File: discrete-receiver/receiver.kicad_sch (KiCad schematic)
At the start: 30 parts, among them J1 His Excellence, J3 External Filter, J7 Her Excellency, T1 H1102NLT, T2 MABA-007159-000000, U5 ADE-1+

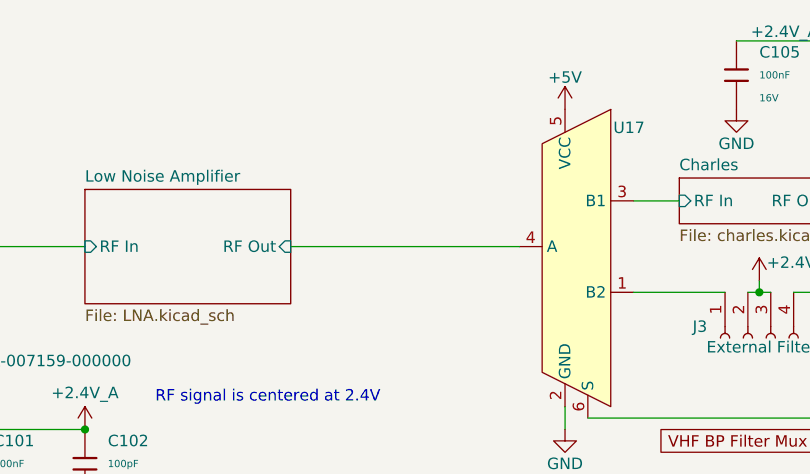
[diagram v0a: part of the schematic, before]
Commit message: Added RF recenter resistor after LNA
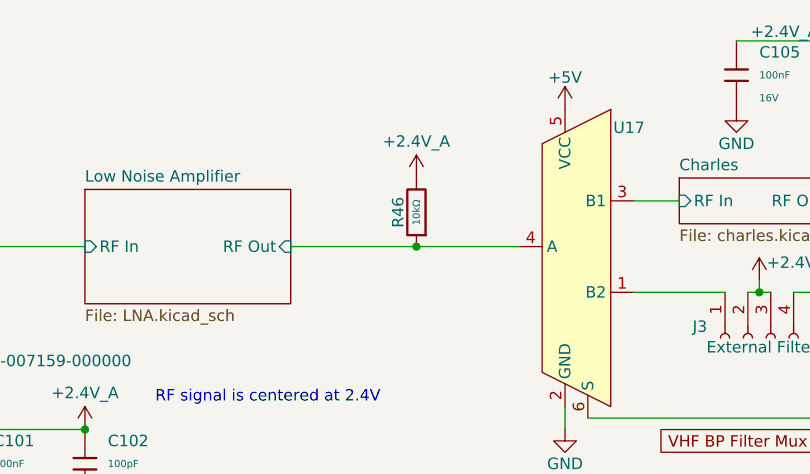
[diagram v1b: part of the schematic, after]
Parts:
- added R46: 10kΩ, PCM_JLCPCB:R_0402, symbol PCM_JLCPCB-Resistors:0402,10kΩ
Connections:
- net +2.4V_A: now also R46.2
- net Low Noise Amplifier/RF Out: now also R46.1

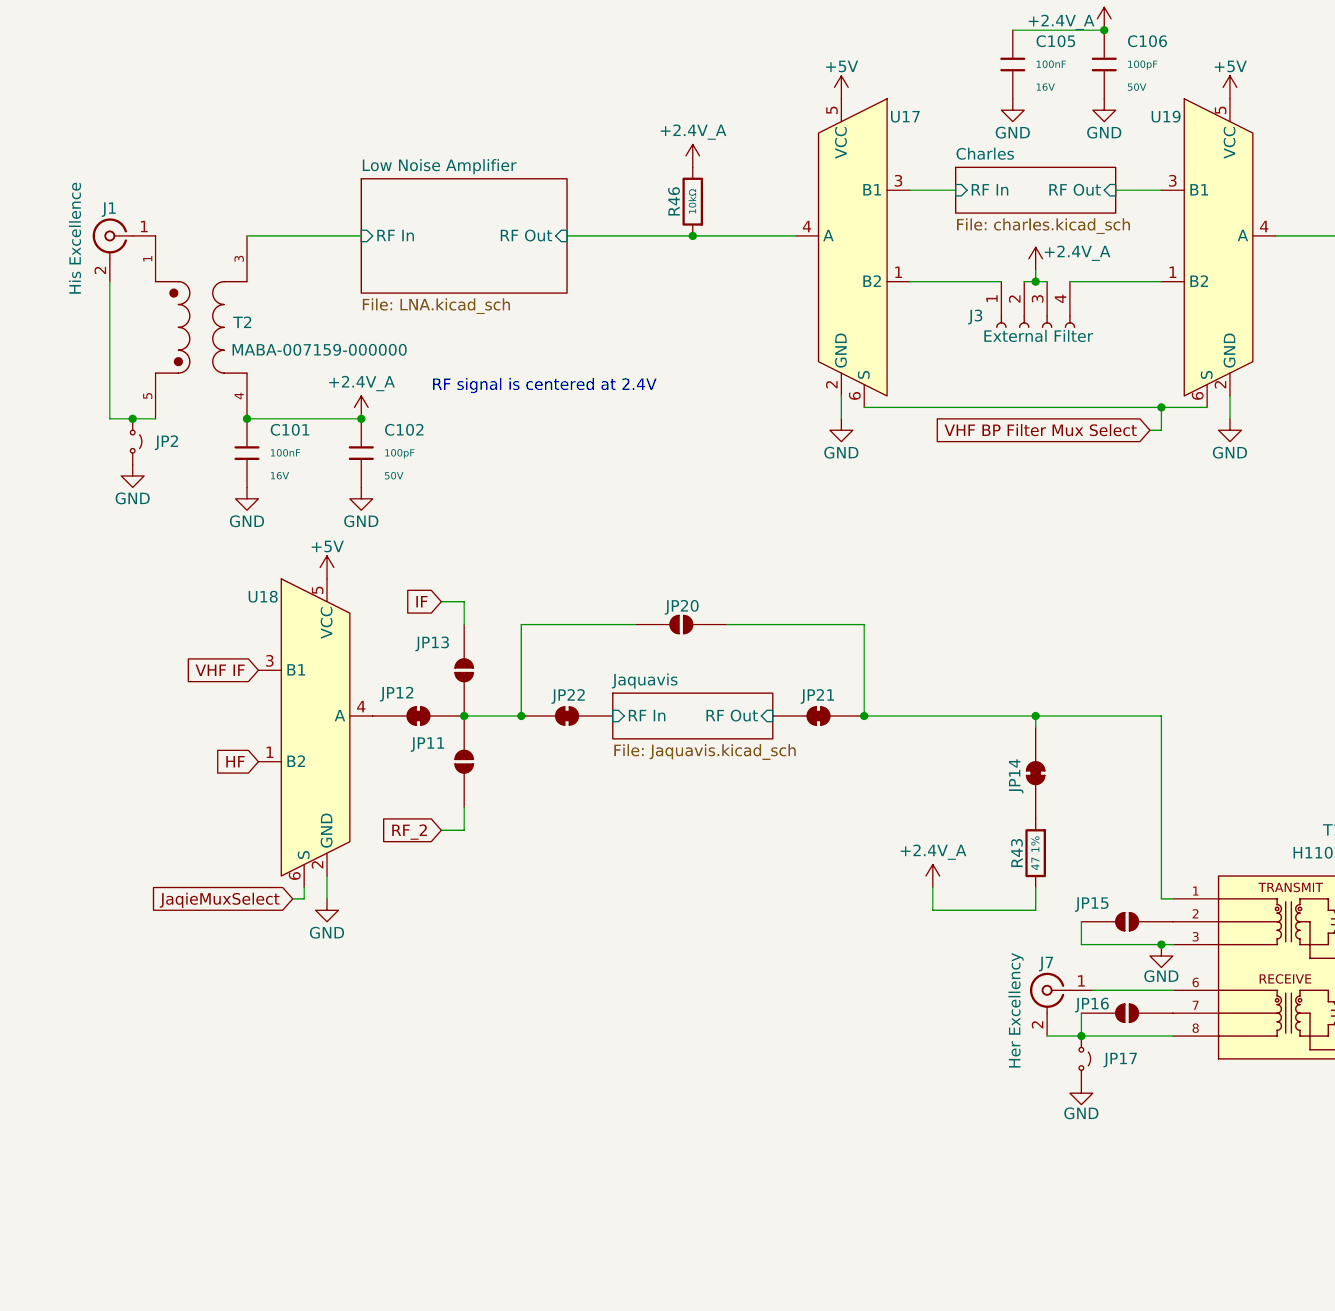
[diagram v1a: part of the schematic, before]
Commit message: Added protection diodes right after both antenna connections
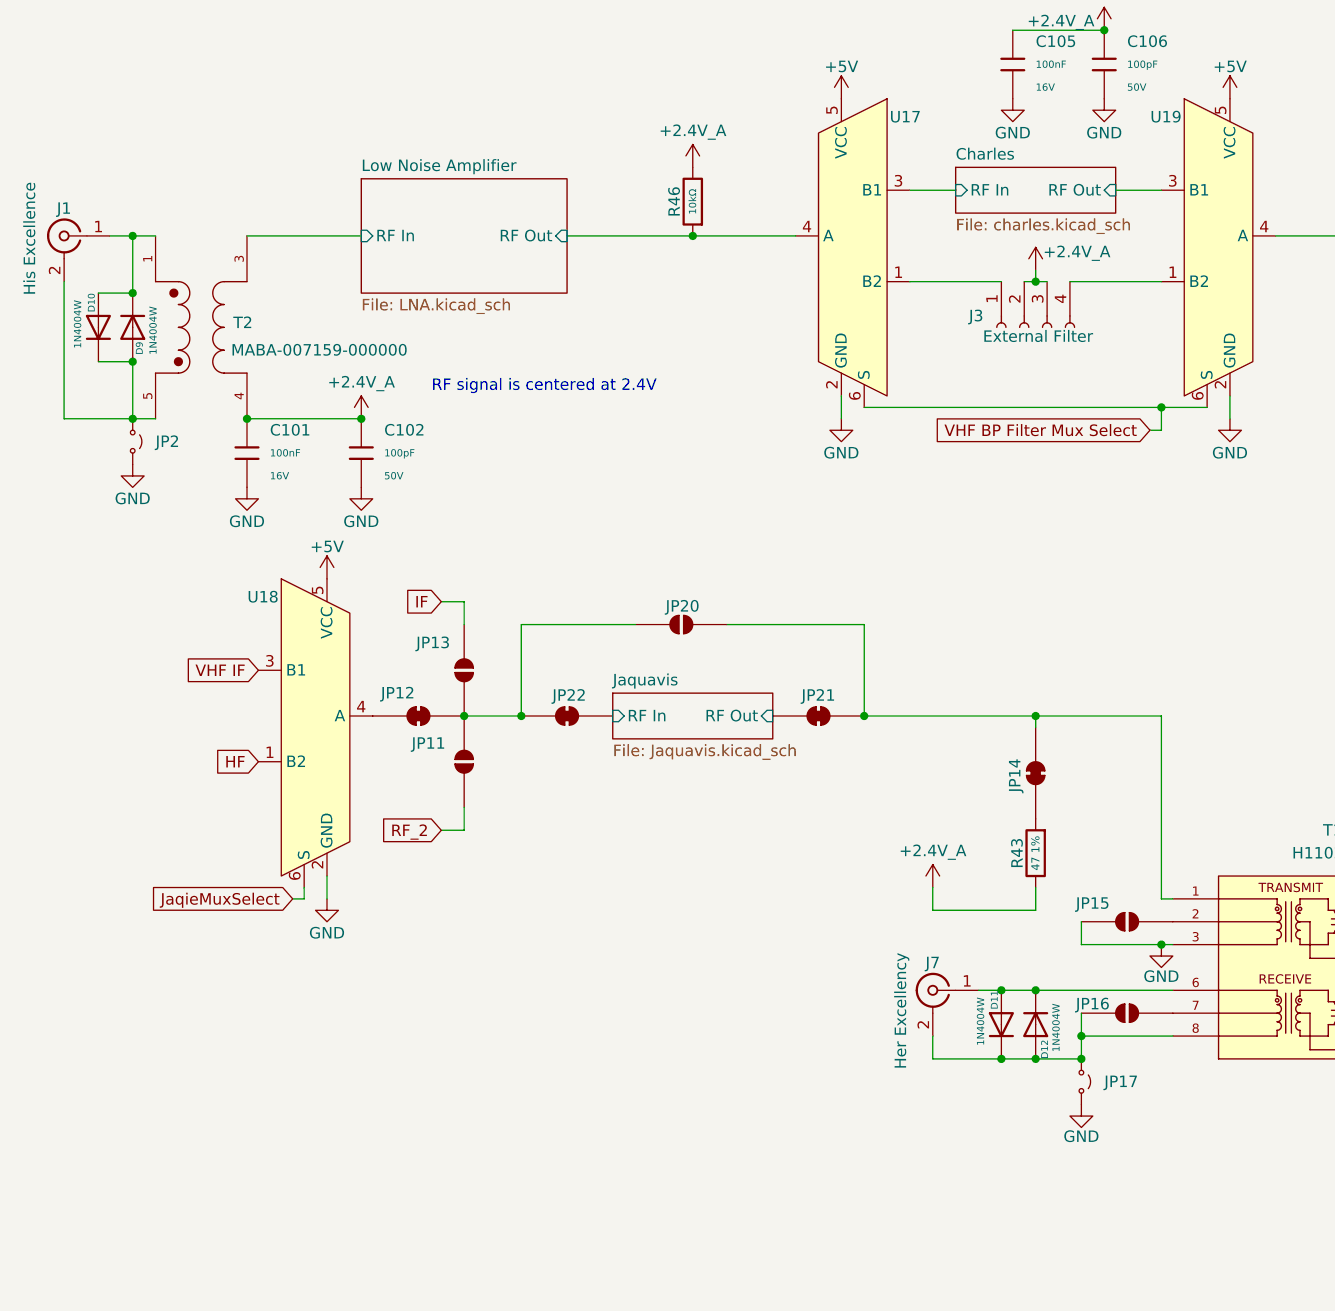
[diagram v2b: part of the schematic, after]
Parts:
- added D10, D11, D12, D9: 1N4004W, PCM_JLCPCB:D_SOD-123FL, symbol PCM_JLCPCB-Diodes:General,1N4004W
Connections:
- net at J7.2 (Ext), JP16.1 (A), JP17.1 (A)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: now also D11.1, D12.2
- net at J7.1 (In), T1.6: now also D11.2, D12.1
- net at J1.2 (Ext), JP2.1 (A), T2.5: now also D10.1, D9.2
- net at J1.1 (In), T2.1: now also D10.2, D9.1
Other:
- moved on the sheet: J1, J7, JP17

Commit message: Made ERC progress
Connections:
- net IF is gone; now on net VHF IF: JP13.2 (B)
- net RF_2 is gone; now on net HF: JP11.1 (A)

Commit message: Initial changes to PCB
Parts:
- J1, J7: footprint Connector_Coaxial:BNC_TEConnectivity_1478204_Vertical -> Frohne Connectors:Conn_Coaxial_Frohne

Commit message: :)
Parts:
- removed J1: His Excellence, Frohne Connectors:Conn_Coaxial_Frohne, symbol Connector:Conn_Coaxial
- removed J7: Her Excellency, Frohne Connectors:Conn_Coaxial_Frohne, symbol Connector:Conn_Coaxial
- added RF1, RF2: 3GHz, EasyEDA_Lib:BNC-TH_DOSIN-801-0051, symbol EasyEDA_Lib:DOSIN-801-0050
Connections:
- net at D11.1, D12.2, JP16.1 (A)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: now also RF1.1, RF1.2, RF1.3, RF1.4
- net at D11.2, D12.1, T1.6: now also RF1.5
- net at D10.1, D9.2, JP2.1 (A)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: now also RF2.1, RF2.2, RF2.3, RF2.4
- net at D10.2, D9.1, T2.1: now also RF2.5
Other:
- note added: "Her Excellency"
- note added: "His Excellence"

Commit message: PCB has begun.
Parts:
- removed C105: 100nF, PCM_JLCPCB:C_0402, symbol PCM_JLCPCB-Capacitors:0402,100nF
- removed C106: 100pF, PCM_JLCPCB:C_0603, symbol PCM_JLCPCB-Capacitors:0603,100pF
- added C69: 100nF, PCM_JLCPCB:C_0402, symbol PCM_JLCPCB-Capacitors:0402,100nF
- added C79: 100pF, PCM_JLCPCB:C_0603, symbol PCM_JLCPCB-Capacitors:0603,100pF
- C101: Price 0.005USD -> 0.004USD; Stock 43509060 -> 20208285
- C102: Manufacturer (none) -> Samsung Electro-Mechanics; Price (none) -> 0.007USD; Stock 6208356 -> 2210509
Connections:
- net +2.4V_A: now also C69.1, C79.1
- net GND: now also C69.2, C79.2

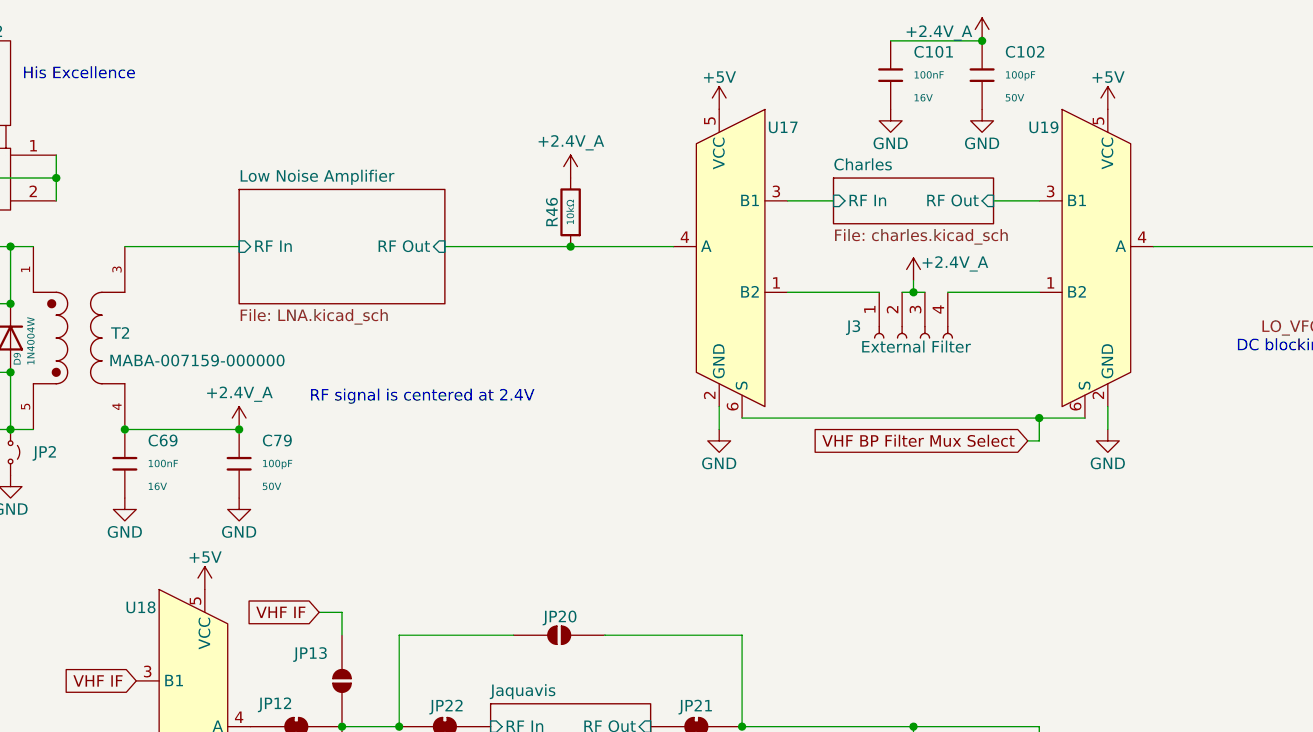
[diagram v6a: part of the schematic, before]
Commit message: PCB Progress
Removed and replaced some residual +5V_A bus labels
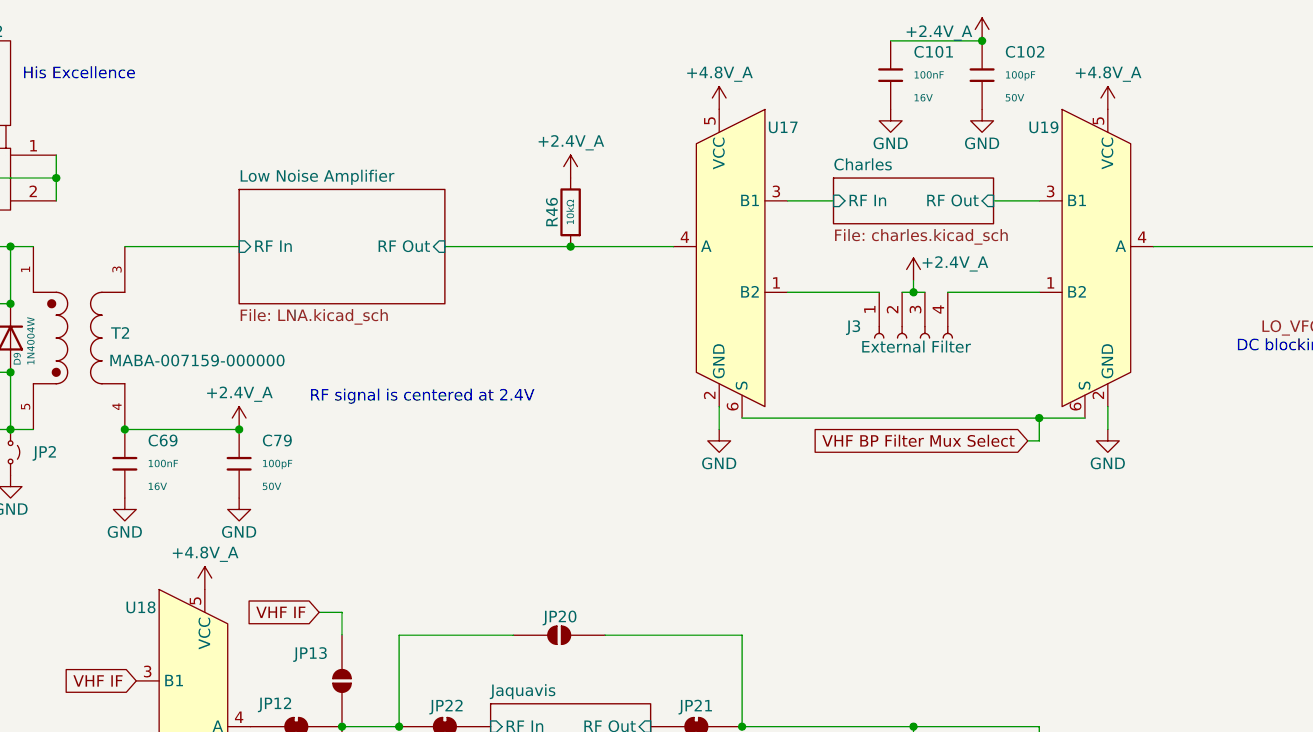
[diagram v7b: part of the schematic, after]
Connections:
- net +5V renamed +4.8V_A

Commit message: Updated JLC part numbers because some parts were out of stock
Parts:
- RF1, RF2: LCSC (none) -> C521210; LCSC Part Name 内孔 BNC 弯头 -> (none); Supplier LCSC -> (none); Supplier Part C521210 -> (none)
